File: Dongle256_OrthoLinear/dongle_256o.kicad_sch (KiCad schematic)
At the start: 65 parts, among them J1 Conn_01x02_Male, SW1 GateronLP, SW10 GateronLP, SW11 GateronLP, SW12 GateronLP, SW13 GateronLP, SW14 GateronLP, SW15 GateronLP, SW16 GateronLP, SW17 GateronLP, SW18 GateronLP, SW19 GateronLP, SW2 GateronLP, SW20 GateronLP, SW21 GateronLP, SW22 GateronLP, SW23 GateronLP, SW24 GateronLP, SW25 GateronLP, SW26 GateronLP, SW27 GateronLP, SW28 GateronLP, SW29 GateronLP, SW3 GateronLP, SW30 GateronLP, SW4 GateronLP, SW5 GateronLP, SW6 GateronLP, SW7 GateronLP, SW8 GateronLP, SW9 GateronLP, U1 NRF52840-DONGLE, U2 NRF52840-DONGLE

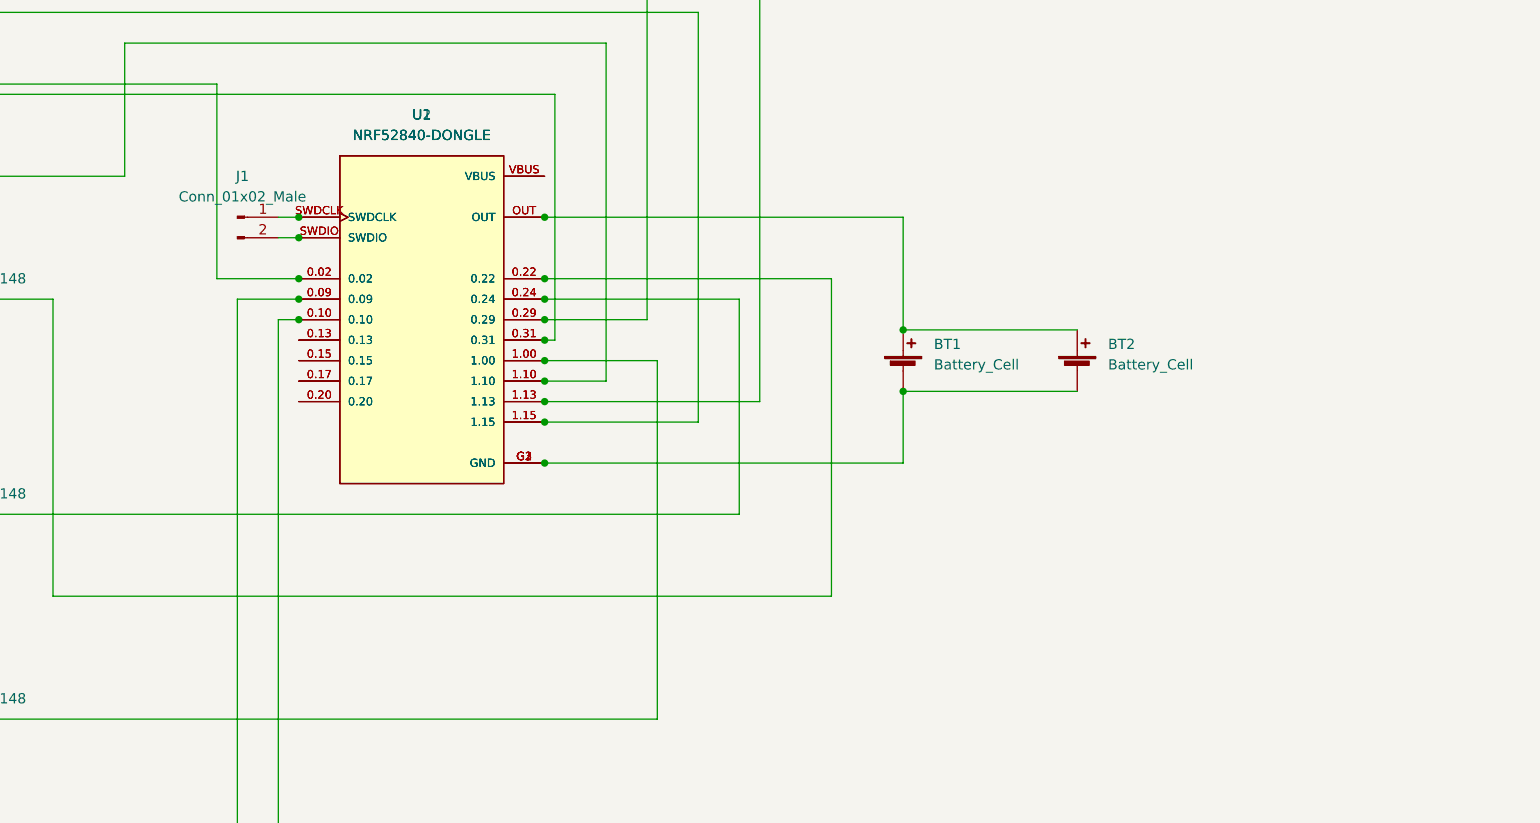
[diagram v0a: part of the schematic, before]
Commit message: Update on off and slider switch
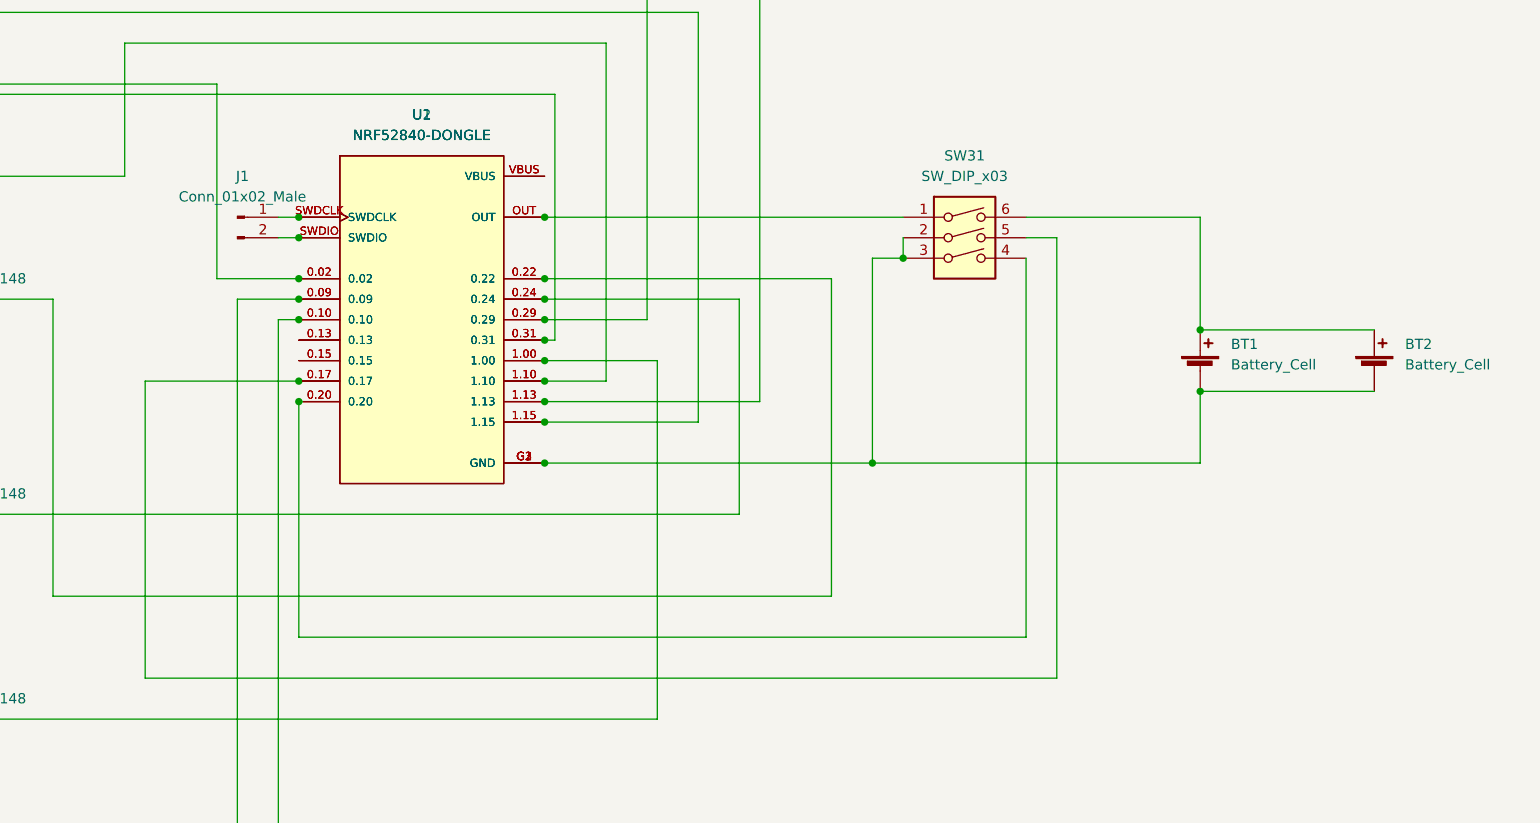
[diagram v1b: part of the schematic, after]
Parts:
- added SW31: SW_DIP_x03, Button_Switch_THT:SW_DIP_SPSTx03_Slide_6.7x9.18mm_W7.62mm_P2.54mm_LowProfile, symbol Switch:SW_DIP_x03
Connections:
- net at BT1.1 (+), BT2.1 (+): now also SW31.6; no longer U1.OUT, U2.OUT
- net at BT1.2 (-), BT2.2 (-), U1.G1 (GND)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: now also SW31.2, SW31.3
- net at U1.0.17, U2.0.17: now also SW31.5
- net at U1.0.20, U2.0.20: now also SW31.4
- new net: SW31.1, U1.OUT, U2.OUT
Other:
- moved on the sheet: BT1, BT2

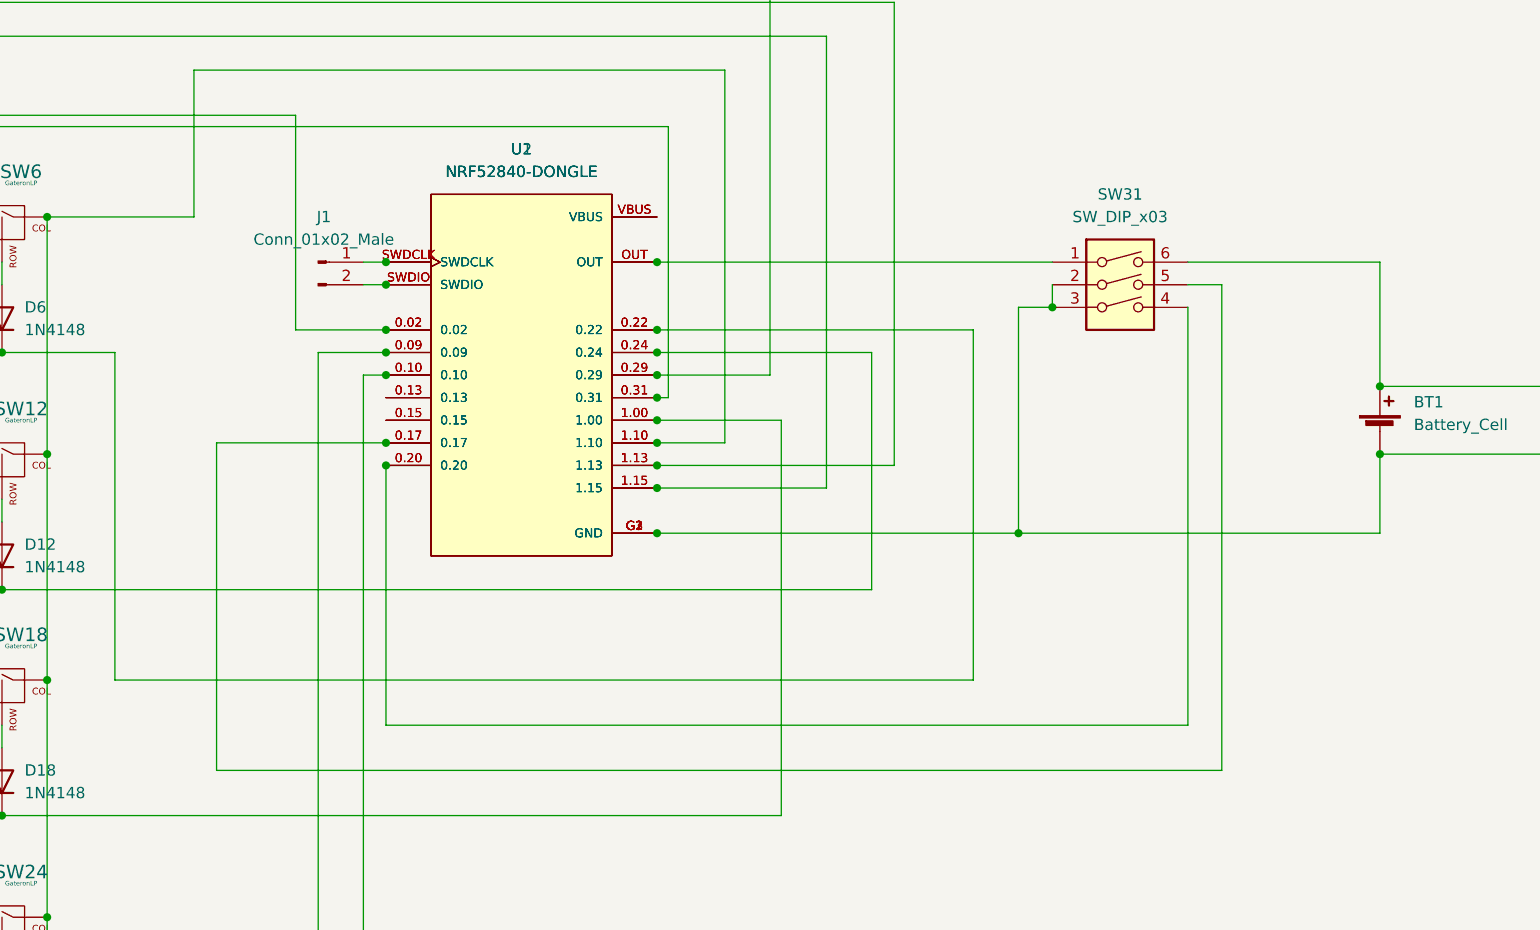
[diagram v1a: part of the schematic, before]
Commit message: Update flashing pads and redo the status switch.
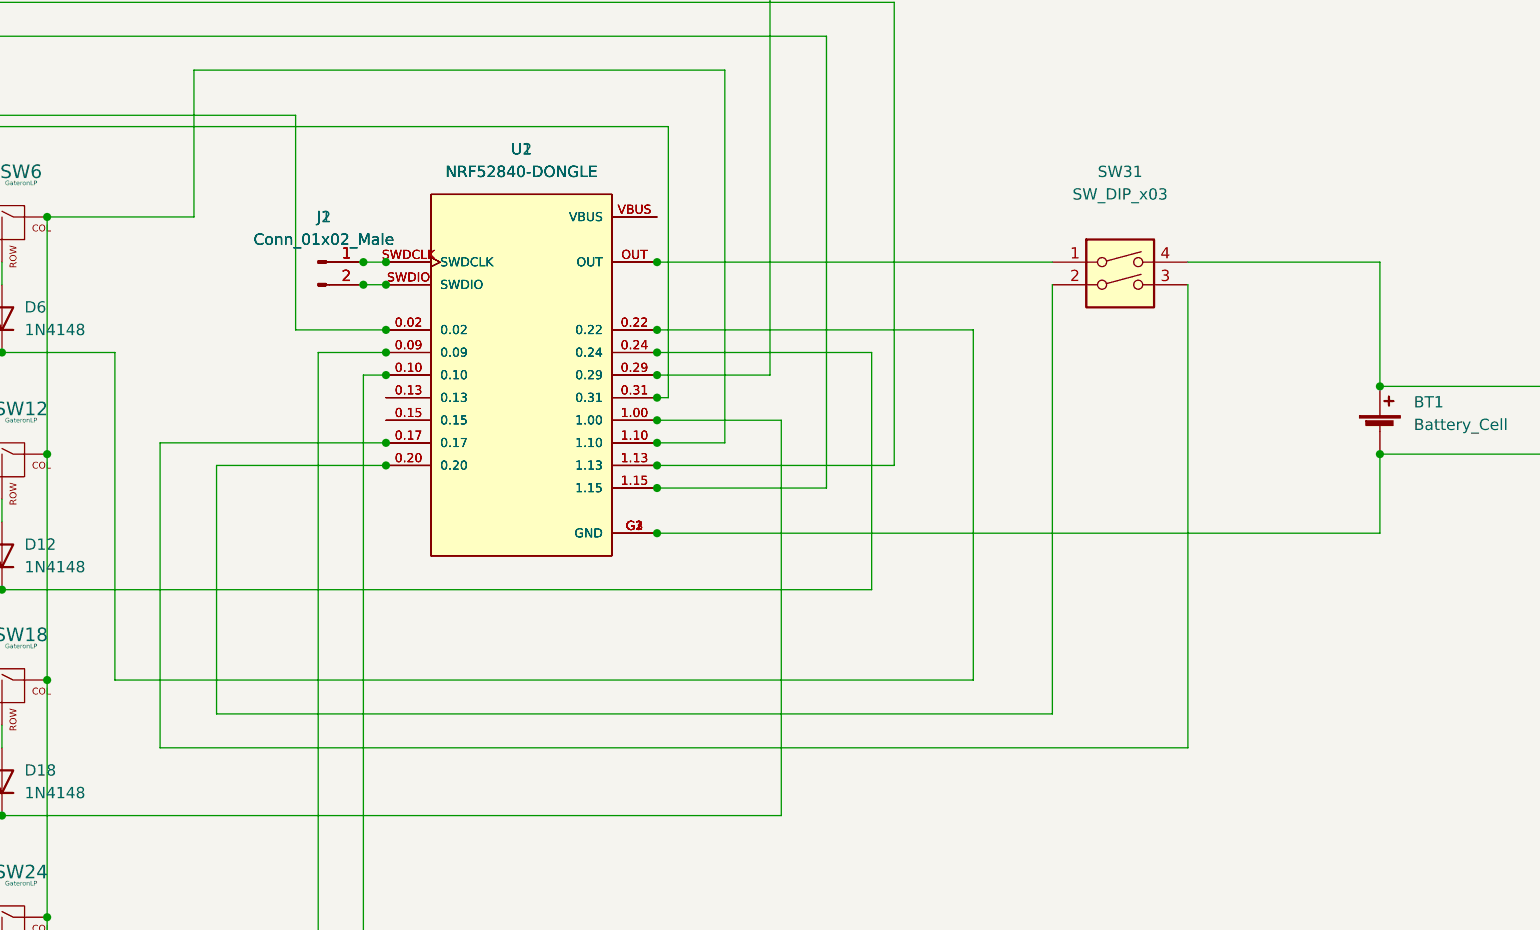
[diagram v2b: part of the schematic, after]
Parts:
- added J2: Conn_01x02_Male, Connector_PinHeader_2.54mm:PinHeader_1x02_P2.54mm_Vertical, symbol Connector:Conn_01x02_Male
- SW31: footprint Button_Switch_THT:SW_DIP_SPSTx03_Slide_6.7x9.18mm_W7.62mm_P2.54mm_LowProfile -> Button_Switch_THT:SW_DIP_SPSTx03_Slide_9.78x9.8mm_W7.62mm_P2.54mm; symbol Switch:SW_DIP_x03 -> Switch:SW_DIP_x02
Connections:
- net at BT1.1 (+), BT2.1 (+): now also SW31.4; no longer SW31.6
- net at BT1.2 (-), BT2.2 (-), U1.G1 (GND)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: no longer SW31.2, SW31.3
- net at U1.0.17, U2.0.17: now also SW31.3; no longer SW31.5
- net at U1.0.20, U2.0.20: now also SW31.2; no longer SW31.4
- net at J1.1 (Pin_1), U1.SWDCLK, U2.SWDCLK: now also J2.1 (Pin_1)
- net at J1.2 (Pin_2), U1.SWDIO, U2.SWDIO: now also J2.2 (Pin_2)
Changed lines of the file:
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@@
   (junction (at 120.65 80.01) (diameter 0) (color 0 0 0 0)
   )
+  (junction (at 177.8 53.34) (diameter 0) (color 0 0 0 0)
+  )
   (junction (at 48.26 80.01) (diameter 0) (color 0 0 0 0)
   )
@@
   (junction (at 177.8 45.72) (diameter 0) (color 0 0 0 0)
   )
+  (junction (at 175.26 35.56) (diameter 0) (color 0 0 0 0)
+  )
   (junction (at 48.26 27.94) (diameter 0) (color 0 0 0 0)
   )
   (junction (at 120.65 54.61) (diameter 0) (color 0 0 0 0)
   )
-  (junction (at 177.8 53.34) (diameter 0) (color 0 0 0 0)
-  )
   (junction (at 208.28 50.8) (diameter 0) (color 0 0 0 0)
   )
+  (junction (at 175.26 33.02) (diameter 0) (color 0 0 0 0)
+  )
   (junction (at 134.62 95.25) (diameter 0) (color 0 0 0 0)
   )
@@
   (junction (at 97.79 69.85) (diameter 0) (color 0 0 0 0)
   )
-  (junction (at 248.92 63.5) (diameter 0) (color 0 0 0 0)
-  )
   (junction (at 60.96 148.59) (diameter 0) (color 0 0 0 0)
   )
@@
   (junction (at 115.57 69.85) (diameter 0) (color 0 0 0 0)
   )
-  (junction (at 252.73 38.1) (diameter 0) (color 0 0 0 0)
-  )
   (junction (at 139.7 106.68) (diameter 0) (color 0 0 0 0)
   )
   (junction (at 66.04 27.94) (diameter 0) (color 0 0 0 0)
   )
+  (junction (at 177.8 55.88) (diameter 0) (color 0 0 0 0)
+  )
   (junction (at 134.62 43.18) (diameter 0) (color 0 0 0 0)
   )
@@
   (junction (at 97.79 43.18) (diameter 0) (color 0 0 0 0)
   )
-  (junction (at 177.8 55.88) (diameter 0) (color 0 0 0 0)
-  )
   (junction (at 83.82 54.61) (diameter 0) (color 0 0 0 0)
   )
@@
     (stroke (width 0) (type default) (color 0 0 0 0))
   )
+  (wire (pts (xy 152.4 87.63) (xy 152.4 53.34))
+    (stroke (width 0) (type default) (color 0 0 0 0))
+  )
   (wire (pts (xy 78.74 121.92) (xy 97.79 121.92))
     (stroke (width 0) (type default) (color 0 0 0 0))
@@
     (stroke (width 0) (type default) (color 0 0 0 0))
   )
-  (wire (pts (xy 267.97 85.09) (xy 267.97 38.1))
-    (stroke (width 0) (type default) (color 0 0 0 0))
-  )
   (wire (pts (xy 134.62 148.59) (xy 175.26 148.59))
     (stroke (width 0) (type default) (color 0 0 0 0))
@@
     (stroke (width 0) (type default) (color 0 0 0 0))
   )
-  (wire (pts (xy 248.92 38.1) (xy 248.92 63.5))
+  (wire (pts (xy 267.97 33.02) (xy 289.56 33.02))
     (stroke (width 0) (type default) (color 0 0 0 0))
   )
@@
     (stroke (width 0) (type default) (color 0 0 0 0))
   )
-  (wire (pts (xy 271.78 35.56) (xy 267.97 35.56))
-    (stroke (width 0) (type default) (color 0 0 0 0))
-  )
-  (wire (pts (xy 208.28 63.5) (xy 248.92 63.5))
-    (stroke (width 0) (type default) (color 0 0 0 0))
-  )
   (wire (pts (xy 66.04 1.27) (xy 220.98 1.27))
     (stroke (width 0) (type default) (color 0 0 0 0))
@@
     (stroke (width 0) (type default) (color 0 0 0 0))
   )
-  (wire (pts (xy 177.8 85.09) (xy 267.97 85.09))
+  (wire (pts (xy 152.4 87.63) (xy 267.97 87.63))
     (stroke (width 0) (type default) (color 0 0 0 0))
   )
@@
     (stroke (width 0) (type default) (color 0 0 0 0))
   )
-  (wire (pts (xy 271.78 90.17) (xy 271.78 35.56))
-    (stroke (width 0) (type default) (color 0 0 0 0))
-  )
   (wire (pts (xy 43.18 148.59) (xy 60.96 148.59))
     (stroke (width 0) (type default) (color 0 0 0 0))
@@
     (stroke (width 0) (type default) (color 0 0 0 0))
   )
-  (wire (pts (xy 177.8 55.88) (xy 177.8 85.09))
-    (stroke (width 0) (type default) (color 0 0 0 0))
-  )
   (wire (pts (xy 215.9 53.34) (xy 208.28 53.34))
     (stroke (width 0) (type default) (color 0 0 0 0))
@@
     (stroke (width 0) (type default) (color 0 0 0 0))
   )
-  (wire (pts (xy 248.92 63.5) (xy 289.56 63.5))
+  (wire (pts (xy 208.28 63.5) (xy 289.56 63.5))
     (stroke (width 0) (type default) (color 0 0 0 0))
   )
@@
     (stroke (width 0) (type default) (color 0 0 0 0))
   )
-  (wire (pts (xy 252.73 38.1) (xy 248.92 38.1))
-    (stroke (width 0) (type default) (color 0 0 0 0))
-  )
   (wire (pts (xy 170.18 121.92) (xy 170.18 43.18))
     (stroke (width 0) (type default) (color 0 0 0 0))
@@
     (stroke (width 0) (type default) (color 0 0 0 0))
   )
+  (wire (pts (xy 252.73 35.56) (xy 252.73 83.82))
+    (stroke (width 0) (type default) (color 0 0 0 0))
+  )
   (wire (pts (xy 120.65 3.81) (xy 120.65 27.94))
     (stroke (width 0) (type default) (color 0 0 0 0))
@@
     (stroke (width 0) (type default) (color 0 0 0 0))
   )
-  (wire (pts (xy 158.75 53.34) (xy 158.75 90.17))
+  (wire (pts (xy 158.75 55.88) (xy 158.75 83.82))
     (stroke (width 0) (type default) (color 0 0 0 0))
   )
@@
     (stroke (width 0) (type default) (color 0 0 0 0))
   )
-  (wire (pts (xy 158.75 90.17) (xy 271.78 90.17))
+  (wire (pts (xy 267.97 87.63) (xy 267.97 35.56))
+    (stroke (width 0) (type default) (color 0 0 0 0))
+  )
+  (wire (pts (xy 152.4 53.34) (xy 177.8 53.34))
+    (stroke (width 0) (type default) (color 0 0 0 0))
+  )
+  (wire (pts (xy 158.75 83.82) (xy 252.73 83.82))
     (stroke (width 0) (type default) (color 0 0 0 0))
   )
@@
     (stroke (width 0) (type default) (color 0 0 0 0))
   )
-  (wire (pts (xy 267.97 33.02) (xy 289.56 33.02))
-    (stroke (width 0) (type default) (color 0 0 0 0))
-  )
-  (wire (pts (xy 252.73 35.56) (xy 252.73 38.1))
-    (stroke (width 0) (type default) (color 0 0 0 0))
-  )
-  (wire (pts (xy 177.8 53.34) (xy 158.75 53.34))
+  (wire (pts (xy 177.8 55.88) (xy 158.75 55.88))
     (stroke (width 0) (type default) (color 0 0 0 0))
   )
@@
     (pin "2")
   )
-  (symbol (lib_id "Switch:SW_DIP_x03") (at 260.35 38.1 0) (unit 1)
-    (in_bom yes) (on_board yes) (fields_autoplaced)
-    (property "Reference" "SW31" (id 0) (at 260.35 25.4 0))
-    (property "Value" "SW_DIP_x03" (id 1) (at 260.35 27.94 0))
-    (property "Footprint" "Button_Switch_THT:SW_DIP_SPSTx03_Slide_6.7x9.18mm_W7.62mm_P2.54mm_LowProfile" (id 2) (at 260.35 38.1 0)
-      (effects (font (size 1.27 1.27)) hide)
-    )
-    (property "Datasheet" "~" (id 3) (at 260.35 38.1 0)
+  (symbol (lib_id "Switch:SW_DIP_x02") (at 260.35 35.56 0) (unit 1)
+    (in_bom yes) (on_board yes) (fields_autoplaced)
+    (property "Reference" "SW31" (id 0) (at 260.35 22.86 0))
+    (property "Value" "SW_DIP_x03" (id 1) (at 260.35 25.4 0))
+    (property "Footprint" "Button_Switch_THT:SW_DIP_SPSTx03_Slide_9.78x9.8mm_W7.62mm_P2.54mm" (id 2) (at 260.35 35.56 0)
+      (effects (font (size 1.27 1.27)) hide)
+    )
+    (property "Datasheet" "~" (id 3) (at 260.35 35.56 0)
       (effects (font (size 1.27 1.27)) hide)
     )
@@
     (pin "3")
     (pin "4")
-    (pin "5")
-    (pin "6")
   )
   (symbol (lib_id "Diode:1N4148") (at 134.62 66.04 90) (unit 1)
@@
     (pin "2")
   )
+  (symbol (lib_id "Connector:Conn_01x02_Male") (at 170.18 33.02 0) (unit 1)
+    (in_bom yes) (on_board yes) (fields_autoplaced)
+    (property "Reference" "J2" (id 0) (at 170.815 27.94 0))
+    (property "Value" "Conn_01x02_Male" (id 1) (at 170.815 30.48 0))
+    (property "Footprint" "Connector_PinHeader_2.54mm:PinHeader_1x02_P2.54mm_Vertical" (id 2) (at 170.18 33.02 0)
+      (effects (font (size 1.27 1.27)) hide)
+    )
+    (property "Datasheet" "~" (id 3) (at 170.18 33.02 0)
+      (effects (font (size 1.27 1.27)) hide)
+    )
+    (pin "1")
+    (pin "2")
+  )
   (symbol (lib_id "Diode:1N4148") (at 134.62 39.37 90) (unit 1)
     (in_bom yes) (on_board yes) (fields_autoplaced)
@@
       (reference "J1") (unit 1) (value "Conn_01x02_Male") (footprint "Connector_PinHeader_2.54mm:PinHeader_1x02_P2.54mm_Vertical")
     )
+    (path "/877fd0e1-439d-4ba8-8e8d-50a7938db2ab"
+      (reference "J2") (unit 1) (value "Conn_01x02_Male") (footprint "Connector_PinHeader_2.54mm:PinHeader_1x02_P2.54mm_Vertical")
+    )
     (path "/68306db6-e9fe-420d-a5be-029e7f2a4533"
       (reference "SW1") (unit 1) (value "GateronLP") (footprint "gateronLowProfile:Gateron_low_profile_reversible")
@@
     )
     (path "/506e433e-e730-43f3-89f9-8cf85e8aea9f"
-      (reference "SW31") (unit 1) (value "SW_DIP_x03") (footprint "Button_Switch_THT:SW_DIP_SPSTx03_Slide_6.7x9.18mm_W7.62mm_P2.54mm_LowProfile")
+      (reference "SW31") (unit 1) (value "SW_DIP_x03") (footprint "Button_Switch_THT:SW_DIP_SPSTx03_Slide_9.78x9.8mm_W7.62mm_P2.54mm")
     )
     (path "/643cddcb-1813-4c85-9ee1-4a412c354744"
